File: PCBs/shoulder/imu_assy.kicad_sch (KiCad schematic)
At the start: 5 parts, among them U2 LSM6DSMTR

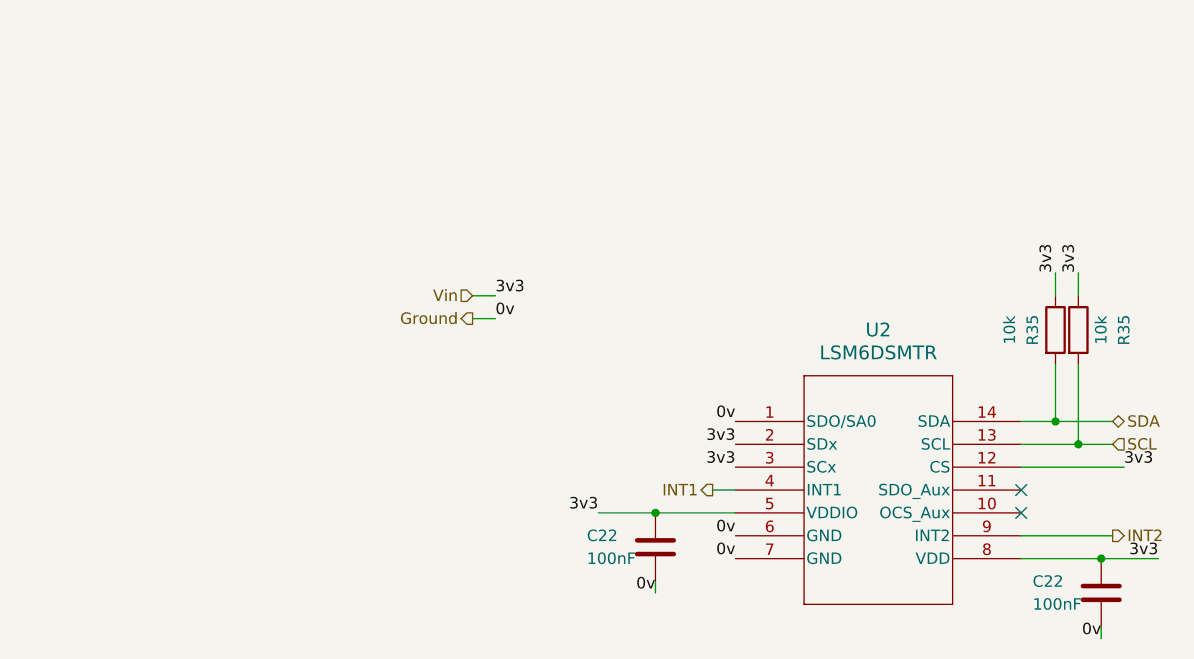
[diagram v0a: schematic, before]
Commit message: Torso all but complete, making bogie before checking the last mark
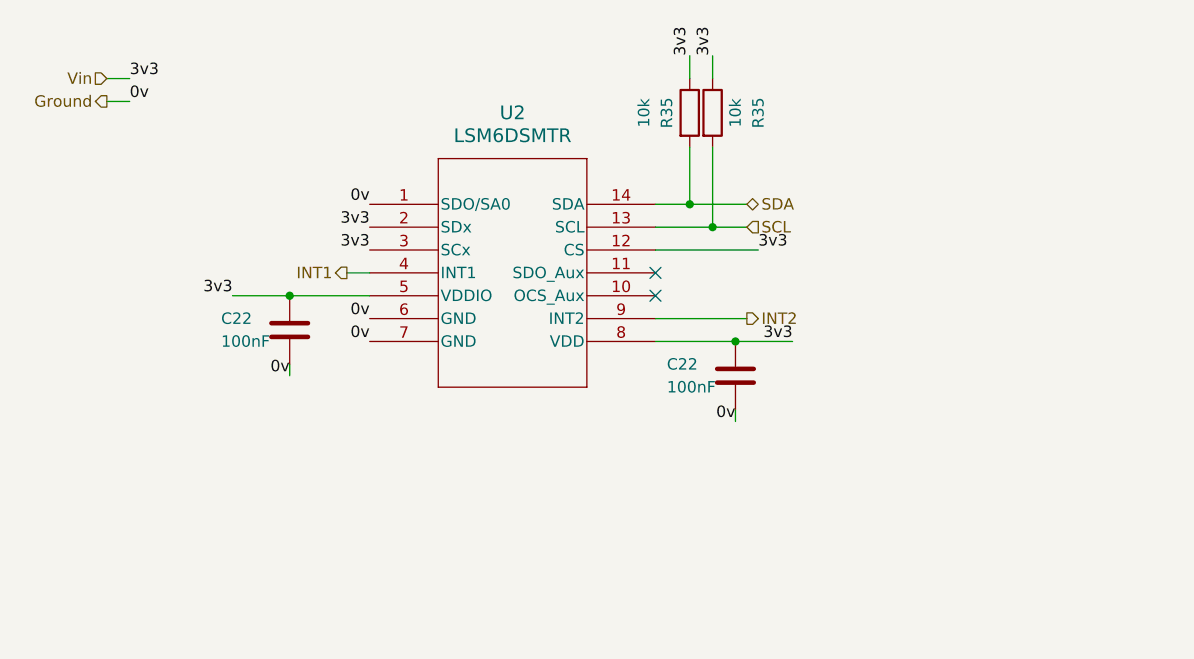
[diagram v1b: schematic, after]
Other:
- moved on the sheet: C22, R35, U2
